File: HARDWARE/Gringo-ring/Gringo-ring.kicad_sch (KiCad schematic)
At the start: 0 parts

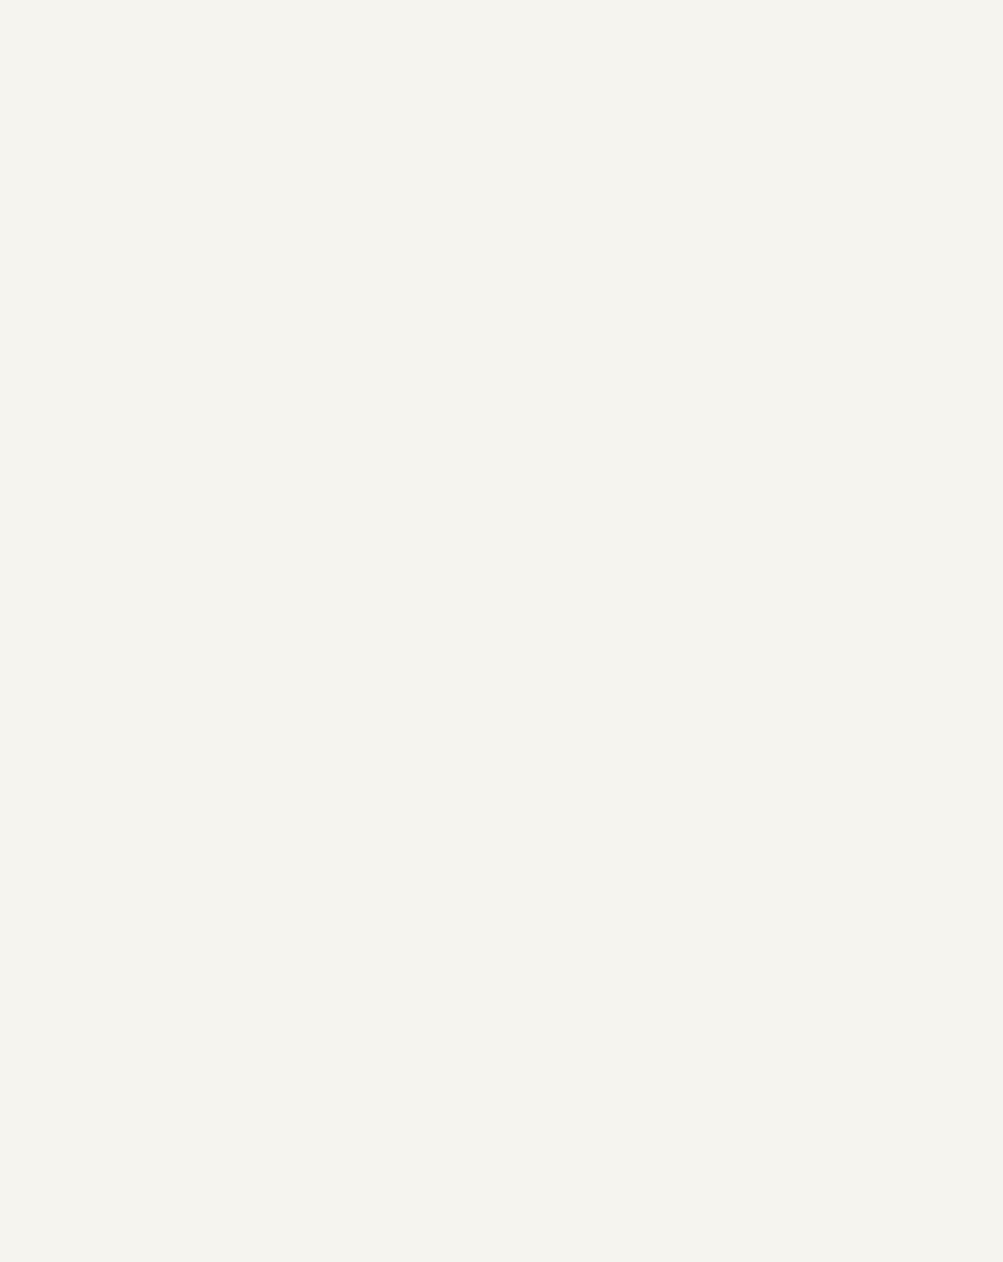
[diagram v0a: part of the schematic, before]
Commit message: Add of schematics pages
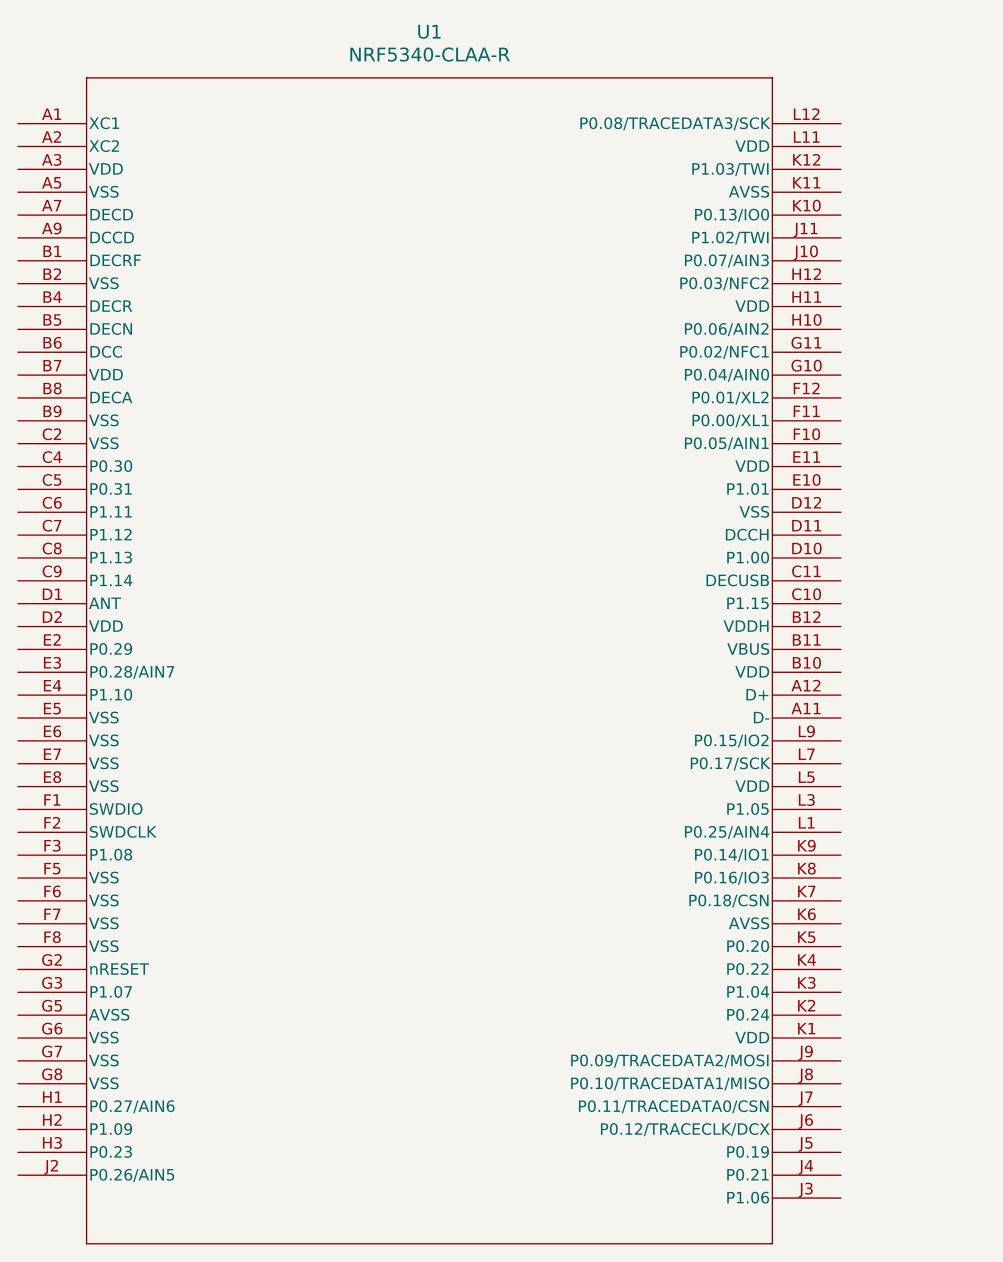
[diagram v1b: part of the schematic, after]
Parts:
- added U1: NRF5340-CLAA-R, WLCSP95_4.390X3.994_NOR, symbol ul_NRF5340-CLAA-R:NRF5340-CLAA-R

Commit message: Commit new organization of files on KiCAD
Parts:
- added J1, J10, J11, J12, J2, J3, J5, J6, J7, J8, J9: Conn_01x06, Connector_PinHeader_2.54mm:PinHeader_1x06_P2.54mm_Vertical, symbol Connector_Generic:Conn_01x06
- added J4: Alim, Connector_PinHeader_2.54mm:PinHeader_1x06_P2.54mm_Vertical, symbol Connector_Generic:Conn_01x06
- added U10: PTPS7A2018PDBVR, DBV0005A-IPC_A, symbol PTPS7A2018PDBVR:PTPS7A2018PDBVR
- added U7: BQ500212ARGZT, BQ500212ARGZT:RGZ0048A, symbol importSnap:BQ500212ARGZT
- added U8: BQ51013ARHLR, RHL20_2P05X3P05, symbol BQ51013ARHLR:BQ51013ARHLR
- added U9: MCP73831T-2ACI/OT, SOT-23-5_MC_MCH, symbol MCP73831T-2ACI-OT:MCP73831T-2ACI_OT
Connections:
- new net: J1.2 (Pin_2), U7.17 (FOD)
- new net: J1.3 (Pin_3), U7.15 (FOD_CAL)
- new net: J1.4 (Pin_4), U7.7 (LED_A)
- new net: J1.5 (Pin_5), U7.8 (LED_B)
- new net: J1.6 (Pin_6), U7.18 (LED_C)
- new net: J11.4 (Pin_4), J12.1 (Pin_1), U10.1 (IN), U9.3 (VBAT)
- new net: J12.3 (Pin_3), U10.3 (EN)
- new net: J12.4 (Pin_4), U10.4 (NC)
- new net: J12.5 (Pin_5), U10.5 (OUT)
- new net: J7.1 (Pin_1), U7.35 (BPCAP)
- new net: J7.2 (Pin_2), U7.11 (DATA)
- new net: J7.3 (Pin_3), U7.10 (CLK)
- new net: J7.4 (Pin_4), U7.46 (V_SENSE)
- new net: J7.5 (Pin_5), U7.2 (T_SENSE)
- new net: J7.6 (Pin_6), U7.42 (I_SENSE)
- new net: J6.3 (Pin_3), U7.1 (PEAK_DET)
- new net: J3.2 (Pin_2), U7.12 (PWM_A)
- new net: J3.3 (Pin_3), U7.13 (PWM_B)
- new net: J3.4 (Pin_4), J3.5 (Pin_5), U7.16 (PMOD), U7.6 (SLEEP)
- new net: J6.5 (Pin_5), U7.21 (DOUT_TX)
- new net: J6.1 (Pin_1), U7.22 (SNOOZE_CHG)
- new net: J6.2 (Pin_2), U7.3 (SNOOZE_CAP)
- new net: J4.3 (Pin_3), U7.31 (GND_31)
- new net: J5.4 (Pin_4), U7.37 (COMM_A+)
- new net: J5.3 (Pin_3), U7.38 (COMM_A–)
- new net: J5.2 (Pin_2), U7.39 (COMM_B+)
- new net: J5.1 (Pin_1), U7.40 (COMM_B-)
- new net: J6.4 (Pin_4), U7.43 (LOSS_THR)
- new net: J6.6 (Pin_6), U7.44 (LED_MODE)
- new net: J5.6 (Pin_6), U7.48 (ADCREF)
- new net: J4.6 (Pin_6), U7.49 (EPAD)
- new net: J5.5 (Pin_5), U7.5 (~{RESET})
- new net: J3.6 (Pin_6), U7.9 (SNOOZE)
- new net: J11.2 (Pin_2), U9.5 (PROG)
- new net: J11.3 (Pin_3), U9.4 (VDD)
- new net: J11.6 (Pin_6), U9.1 (STAT)
- new net: J8.1 (Pin_1), U8.13 (TS-CTRL)
- new net: J8.2 (Pin_2), U8.12 (ILIM)
- new net: J8.3 (Pin_3), U8.11 (EN2)
- new net: J10.1 (Pin_1), U8.10 (EN1/TERM)
- new net: J10.2 (Pin_2), U8.9 (AD)
- new net: J10.3 (Pin_3), U8.8 (*AD-EN)
- new net: J10.4 (Pin_4), U8.7 (*CHG)
- new net: J9.1 (Pin_1), U8.6 (COM1)
- new net: J9.3 (Pin_3), U8.5 (CLMP1)
- new net: J9.4 (Pin_4), U8.4 (OUT)
- new net: J9.5 (Pin_5), U8.3 (BOOT1)
- new net: J2.1 (Pin_1), J9.6 (Pin_6), U8.19 (AC2), U8.2 (AC1)
- new net: J2.2 (Pin_2), U8.18 (RECT)
- new net: J2.3 (Pin_3), U8.17 (BOOT2)
- new net: J2.4 (Pin_4), U8.16 (CLMP2)
- new net: J2.5 (Pin_5), U8.15 (COM2)
- new net: J2.6 (Pin_6), U8.14 (FOD)
- new net GND: J11.5 (Pin_5), J12.2 (Pin_2), J4.4 (Pin_4), J4.5 (Pin_5), J8.4 (Pin_4), J8.5 (Pin_5), J8.6 (Pin_6), U10.2 (GND), U7.32 (GND), U7.36 (GND), U7.47 (GND), U8.1 (PGND), U8.20 (PGND), U8.21 (EPAD), U9.2 (VSS)
- new net V33A: J4.1 (Pin_1), U7.34 (V33A)
- new net V33D: J4.2 (Pin_2), U7.33 (V33D)
- no-connect marks 0 -> 21
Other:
- sheet feuille2 renamed Sensors
- added sheet Actuator (actuator.kicad_sch)
- added sheet Alim_Part (alim_part.kicad_sch)
- moved on the sheet: U1
